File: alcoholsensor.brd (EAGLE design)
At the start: 64.1 x 62.9 mm, 23 parts, among them IC2 7805TV

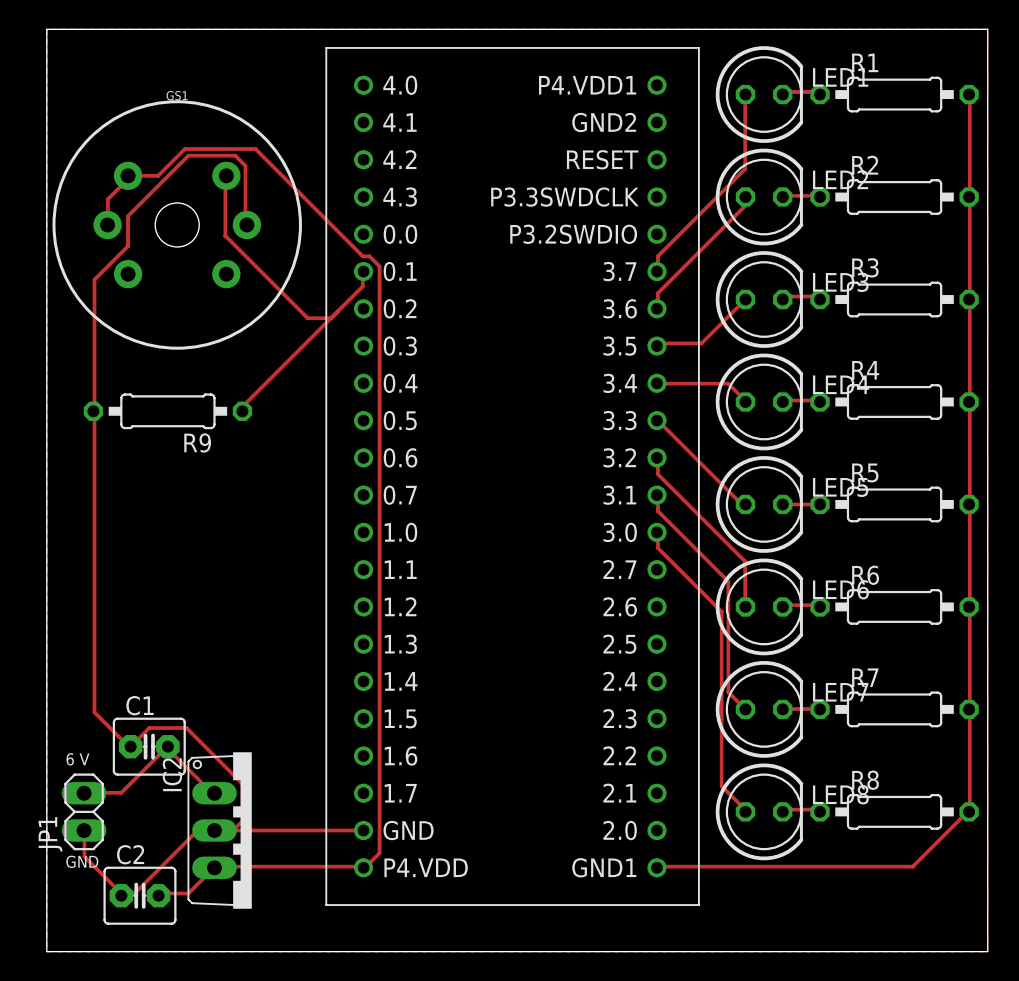
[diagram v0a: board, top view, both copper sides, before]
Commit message: Improved design (made smaller)
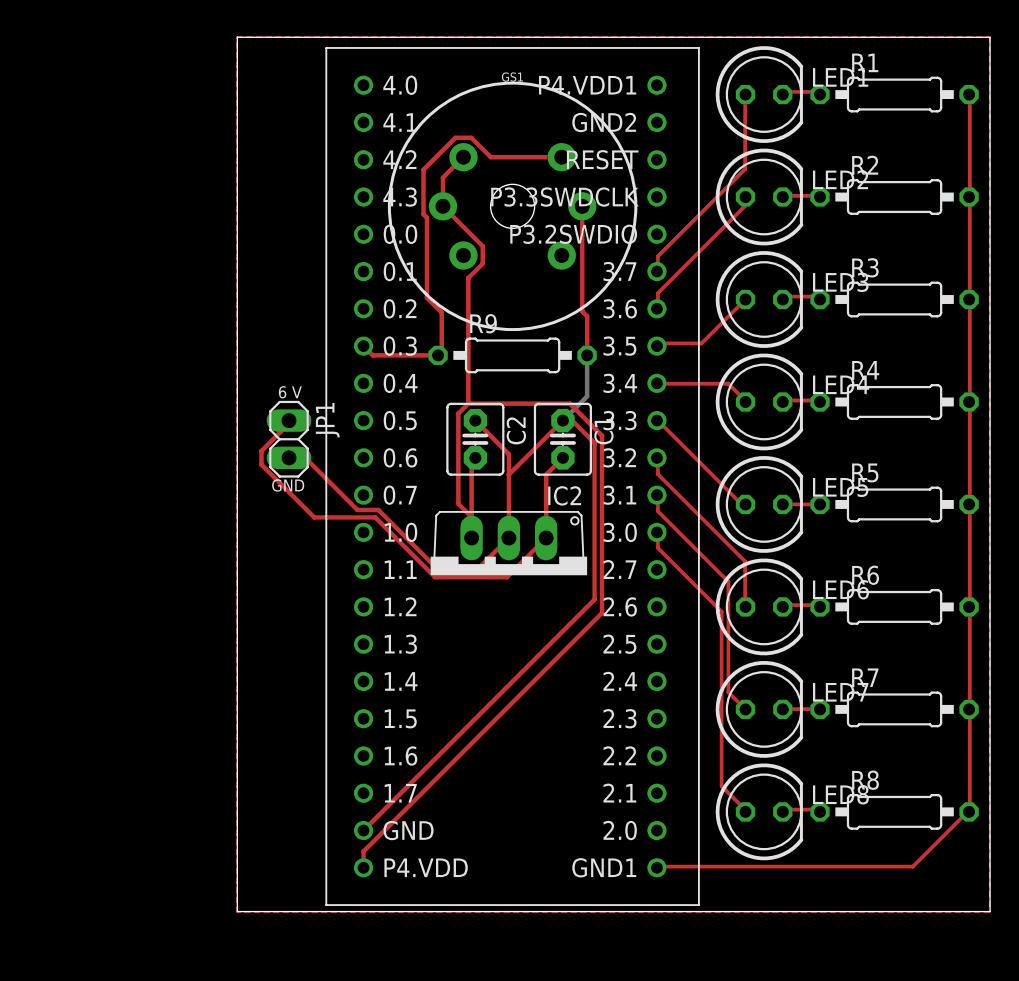
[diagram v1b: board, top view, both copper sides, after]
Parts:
- moved C2 38.6 mm to (47.0, 55.9), turned to 270 degrees
- moved C1 35.1 mm to (53.0, 55.9), turned to 270 degrees
- moved JP1 29.0 mm to (34.3, 55.9), turned to 270 degrees
- moved IC2 24.7 mm to (49.3, 46.6), turned to 180 degrees
- moved R9 23.8 mm to (49.5, 61.6), turned to 0 degrees
- moved GS1 22.9 mm to (49.5, 71.8)
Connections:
- removed net N$20 (its old number): GS1.B1, R9.1, U$1.0.1
- new net N$18: C1.2, IC2.1, JP1.1
- net N$21: now also GS1.B1, R9.1, U$1.0.3; no longer C1.2, IC2.1, JP1.2
- net N$22: now also JP1.2; no longer JP1.1
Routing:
- net N$18: track 0.00 -> 33.4 mm
- net N$20 (its old number): track 27.3 -> 0.00 mm
- net N$21: track 11.6 -> 29.5 mm
- net N$22: track 89.3 -> 84.3 mm
- net N$20: track 81.4 -> 80.5 mm
- added copper zone on layer 1, net N$19
- removed copper zone on layer 1, net GND
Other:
- board size 64.1 x 62.9 mm -> 51.3 x 59.6 mm
